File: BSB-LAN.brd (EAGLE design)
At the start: 51 x 28 mm, 22 parts, among them Q1 BC847, Q2 BC857

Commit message: Add OSHW Logo
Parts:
- added U$3: OSHW-LOGOM, BSB-LAN:OSHW-LOGO-M
- U$1: device CompanyLogos:WARN-TINY -> BSB-LAN:WARN-TINY
- U$2: device CompanyLogos:ESD-TINY -> BSB-LAN:ESD-TINY
- moved U$2 1.41 mm to (40.0, 4.00), turned to 90 degrees
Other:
- board text added: "Open Hardware"
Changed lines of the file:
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@@
 <layer number="14" name="Route14" color="1" fill="6" visible="no" active="no"/>
 <layer number="15" name="Route15" color="4" fill="6" visible="no" active="no"/>
-<layer number="16" name="Bottom" color="1" fill="1" visible="no" active="yes"/>
+<layer number="16" name="Bottom" color="1" fill="1" visible="yes" active="yes"/>
 <layer number="17" name="Pads" color="2" fill="1" visible="yes" active="yes"/>
 <layer number="18" name="Vias" color="2" fill="1" visible="yes" active="yes"/>
@@
 <layer number="20" name="Dimension" color="15" fill="1" visible="yes" active="yes"/>
 <layer number="21" name="tPlace" color="7" fill="1" visible="yes" active="yes"/>
-<layer number="22" name="bPlace" color="7" fill="1" visible="no" active="yes"/>
+<layer number="22" name="bPlace" color="7" fill="1" visible="yes" active="yes"/>
 <layer number="23" name="tOrigins" color="15" fill="1" visible="yes" active="yes"/>
-<layer number="24" name="bOrigins" color="15" fill="1" visible="no" active="yes"/>
+<layer number="24" name="bOrigins" color="15" fill="1" visible="yes" active="yes"/>
 <layer number="25" name="tNames" color="7" fill="1" visible="yes" active="yes"/>
-<layer number="26" name="bNames" color="7" fill="1" visible="no" active="yes"/>
+<layer number="26" name="bNames" color="7" fill="1" visible="yes" active="yes"/>
 <layer number="27" name="tValues" color="7" fill="1" visible="no" active="yes"/>
 <layer number="28" name="bValues" color="7" fill="1" visible="no" active="yes"/>
 <layer number="29" name="tStop" color="7" fill="3" visible="yes" active="yes"/>
-<layer number="30" name="bStop" color="7" fill="6" visible="no" active="yes"/>
+<layer number="30" name="bStop" color="7" fill="6" visible="yes" active="yes"/>
 <layer number="31" name="tCream" color="7" fill="4" visible="no" active="yes"/>
 <layer number="32" name="bCream" color="7" fill="5" visible="no" active="yes"/>
@@
 <layer number="38" name="bTest" color="7" fill="1" visible="no" active="yes"/>
 <layer number="39" name="tKeepout" color="4" fill="11" visible="yes" active="yes"/>
-<layer number="40" name="bKeepout" color="1" fill="11" visible="no" active="yes"/>
+<layer number="40" name="bKeepout" color="1" fill="11" visible="yes" active="yes"/>
 <layer number="41" name="tRestrict" color="4" fill="10" visible="yes" active="yes"/>
-<layer number="42" name="bRestrict" color="1" fill="10" visible="no" active="yes"/>
+<layer number="42" name="bRestrict" color="1" fill="10" visible="yes" active="yes"/>
 <layer number="43" name="vRestrict" color="2" fill="10" visible="no" active="yes"/>
 <layer number="44" name="Drills" color="7" fill="1" visible="no" active="yes"/>
-<layer number="45" name="Holes" color="7" fill="1" visible="no" active="yes"/>
+<layer number="45" name="Holes" color="7" fill="1" visible="yes" active="yes"/>
 <layer number="46" name="Milling" color="3" fill="1" visible="no" active="yes"/>
 <layer number="47" name="Measures" color="7" fill="1" visible="no" active="yes"/>
-<layer number="48" name="Document" color="7" fill="1" visible="no" active="yes"/>
+<layer number="48" name="Document" color="7" fill="1" visible="yes" active="yes"/>
 <layer number="49" name="Reference" color="7" fill="1" visible="no" active="yes"/>
 <layer number="50" name="dxf" color="7" fill="1" visible="no" active="no"/>
@@
 <layer number="59" name="tCarbon" color="7" fill="1" visible="no" active="no"/>
 <layer number="60" name="bCarbon" color="7" fill="1" visible="no" active="no"/>
+<layer number="88" name="SimResults" color="9" fill="1" visible="yes" active="yes"/>
+<layer number="89" name="SimProbes" color="9" fill="1" visible="yes" active="yes"/>
 <layer number="90" name="Modules" color="7" fill="1" visible="no" active="yes"/>
 <layer number="91" name="Nets" color="2" fill="1" visible="no" active="no"/>
@@
 <text x="25.1" y="1.3" size="1" layer="21" font="vector" ratio="15" align="center">github/fredlcore/BSB-LAN</text>
 <text x="7" y="26" size="1" layer="22" font="vector" ratio="15" rot="MR180" align="center">JLCJLCJLC</text>
+<text x="43.4" y="24.95" size="0.8" layer="21" font="vector" ratio="15" rot="R90" align="center">Open
+Hardware</text>
 </plain>
 <attributes>
@@
 <attribute name="LCSC_PART" value="C17888" x="14.4" y="19" size="1.778" layer="27" display="off"/>
 </element>
-<element name="U$1" library="CompanyLogos" package="WARN-TINY" value="" x="4" y="3"/>
-<element name="U$2" library="CompanyLogos" package="ESD-TINY" value="" x="41" y="5"/>
+<element name="U$1" library="BSB-LAN" package="WARN-TINY" value="" x="4" y="3"/>
+<element name="U$2" library="BSB-LAN" package="ESD-TINY" value="" x="40" y="4" rot="R90"/>
+<element name="U$3" library="BSB-LAN" package="OSHW-LOGO-M" value="OSHW-LOGOM" x="40" y="25" rot="R90"/>
 </elements>
 <signals>

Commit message: Update Libraries in basic BSB-LAN design
Bring up to date with JLC export attributes.
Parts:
- U$3: value OSHW-LOGOM -> DNI
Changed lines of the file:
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@@
 <attribute name="LCSC_PART" value="C130417" x="-23.76" y="54.39" size="1.778" layer="27" rot="R180" display="off"/>
 <attribute name="NAME" x="15.4945" y="21.113" size="1" layer="25" font="vector" ratio="15" align="center"/>
+<attribute name="JLC_ROT" value="270" x="18.15" y="20.1" size="1.778" layer="27" rot="R180" display="off"/>
 </element>
 <element name="Q2" library="BSB-LAN" package="SOT23-BEC" value="BC857" x="34.6" y="18.15" smashed="yes" rot="R90">
 <attribute name="LCSC_PART" value="C426782" x="73.97" y="33.39" size="1.778" layer="27" rot="R90" display="off"/>
 <attribute name="NAME" x="33.5445" y="20.513" size="1" layer="25" font="vector" ratio="15" align="center"/>
+<attribute name="JLC_ROT" value="270" x="34.6" y="18.15" size="1.778" layer="27" rot="R90" display="off"/>
 </element>
 <element name="UEXT" library="BSB-LAN" package="ML10F" value="" x="41" y="14" smashed="yes" rot="MR270">
@@
 <attribute name="LCSC_PART" value="C84256" x="57.47" y="29.32" size="1.778" layer="27" rot="R90" display="off"/>
 <attribute name="NAME" x="18.1" y="7.445" size="1" layer="25" ratio="15" rot="R180" align="center"/>
+<attribute name="JLC_ROT" value="270" x="18.1" y="9" size="1.778" layer="27" rot="R90" display="off"/>
 </element>
 <element name="R3" library="BSB-LAN" package="R0805" value="330R" x="32.95" y="14.45" smashed="yes" rot="R270">
@@
 <element name="U$1" library="BSB-LAN" package="WARN-TINY" value="" x="4" y="3"/>
 <element name="U$2" library="BSB-LAN" package="ESD-TINY" value="" x="40" y="4" rot="R90"/>
-<element name="U$3" library="BSB-LAN" package="OSHW-LOGO-M" value="OSHW-LOGOM" x="40" y="25" rot="R90"/>
+<element name="U$3" library="BSB-LAN" package="OSHW-LOGO-M" value="DNI" x="40" y="25" rot="R90">
+<attribute name="VALUE" value="DNI" x="40" y="25" size="1.778" layer="27" rot="R90" display="off"/>
+</element>
 </elements>
 <signals>

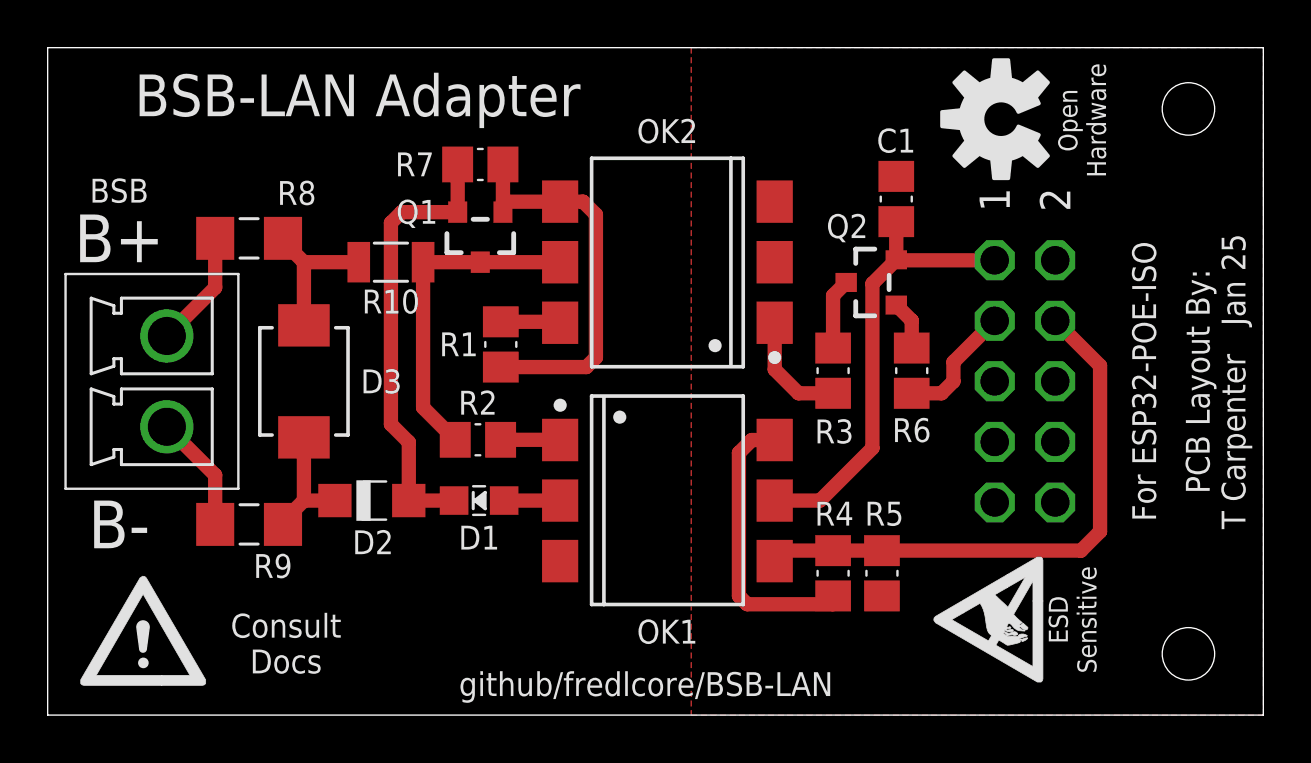
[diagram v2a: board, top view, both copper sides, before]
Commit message: Add missing pull-down to BSB-LAN adapter
4.7k on the TX pin to assist with boot issues on the Olimex dev kit.
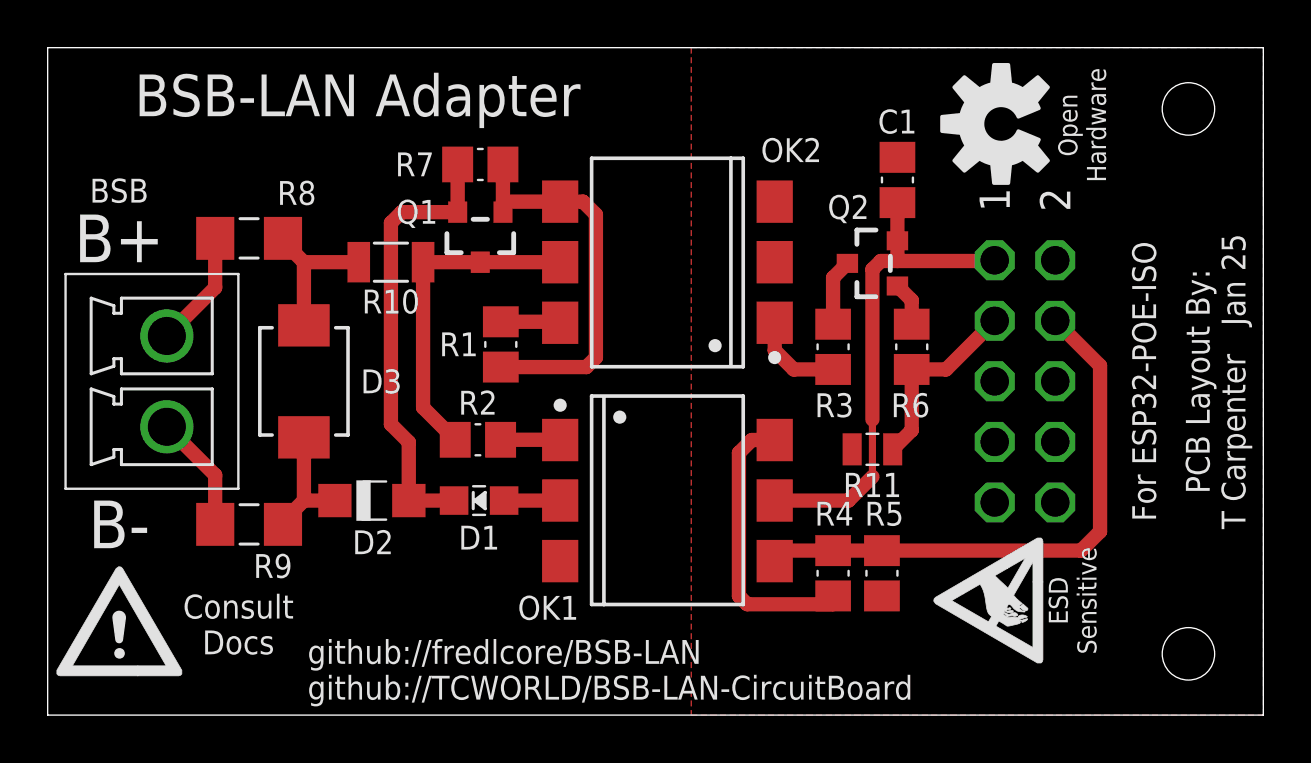
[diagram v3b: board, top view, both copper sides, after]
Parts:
- added R11: 4.7k, BSB-LAN:R0805L
- moved U$1 1.08 mm to (3.00, 3.40)
- moved R3 1.00 mm to (33.0, 15.4)
- moved R6 1.00 mm to (36.2, 15.4)
- moved C1 0.80 mm to (35.6, 22.4)
- moved Q2 0.80 mm to (34.6, 18.9)
- moved U$2 0.80 mm to (40.0, 4.80)
- moved U$3 0.20 mm to (40.0, 24.8)
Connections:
- net GND: now also R11.2
- net TXD: now also R11.1
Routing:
- net TXD: track 5.21 -> 8.01 mm
- net VCC: track 19.1 -> 21.0 mm
- net TXD-A: track 4.82 -> 3.94 mm
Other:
- board text added: "github://fredlcore/BSB-LAN github://TCWORLD/BSB-LAN-CircuitBoard"
- board text removed: "github/fredlcore/BSB-LAN"

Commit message: Adjust Silkscreen
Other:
- board text added: "BSB to UEXT Adapter"
- board text added: "github://TCWORLD/BSB-Interface-PCBs"
- board text removed: "BSB-LAN Adapter"
- board text removed: "github://fredlcore/BSB-LAN github://TCWORLD/BSB-LAN-CircuitBoard"
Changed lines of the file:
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@@
 <hole x="47.858" y="25.43" drill="2.2"/>
 <hole x="47.858" y="2.57" drill="2.2"/>
-<text x="13" y="26" size="1.75" layer="21" font="vector" ratio="15" align="center">BSB-LAN Adapter</text>
+<text x="16" y="26" size="1.75" layer="21" font="vector" ratio="15" align="center">BSB to UEXT Adapter</text>
 <text x="49" y="14" size="1" layer="21" font="vector" ratio="15" rot="R90" align="center">PCB Layout By:
 T Carpenter   Jan 25</text>
@@
 Docs</text>
 <text x="46" y="14" size="1" layer="21" font="vector" ratio="15" rot="R90" align="center">For ESP32-POE-ISO</text>
-<text x="10.9" y="1.9" size="1" layer="21" font="vector" ratio="15" align="center-left">github://fredlcore/BSB-LAN
-github://TCWORLD/BSB-LAN-CircuitBoard</text>
+<text x="10.9" y="1.9" size="1" layer="21" font="vector" ratio="15" align="center-left">github://TCWORLD/BSB-Interface-PCBs</text>
 <text x="7" y="26" size="1" layer="22" font="vector" ratio="15" rot="MR180" align="center">JLCJLCJLC</text>
 <text x="43.4" y="24.75" size="0.8" layer="21" font="vector" ratio="15" rot="R90" align="center">Open
